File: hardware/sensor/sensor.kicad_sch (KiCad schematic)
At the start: 12 parts

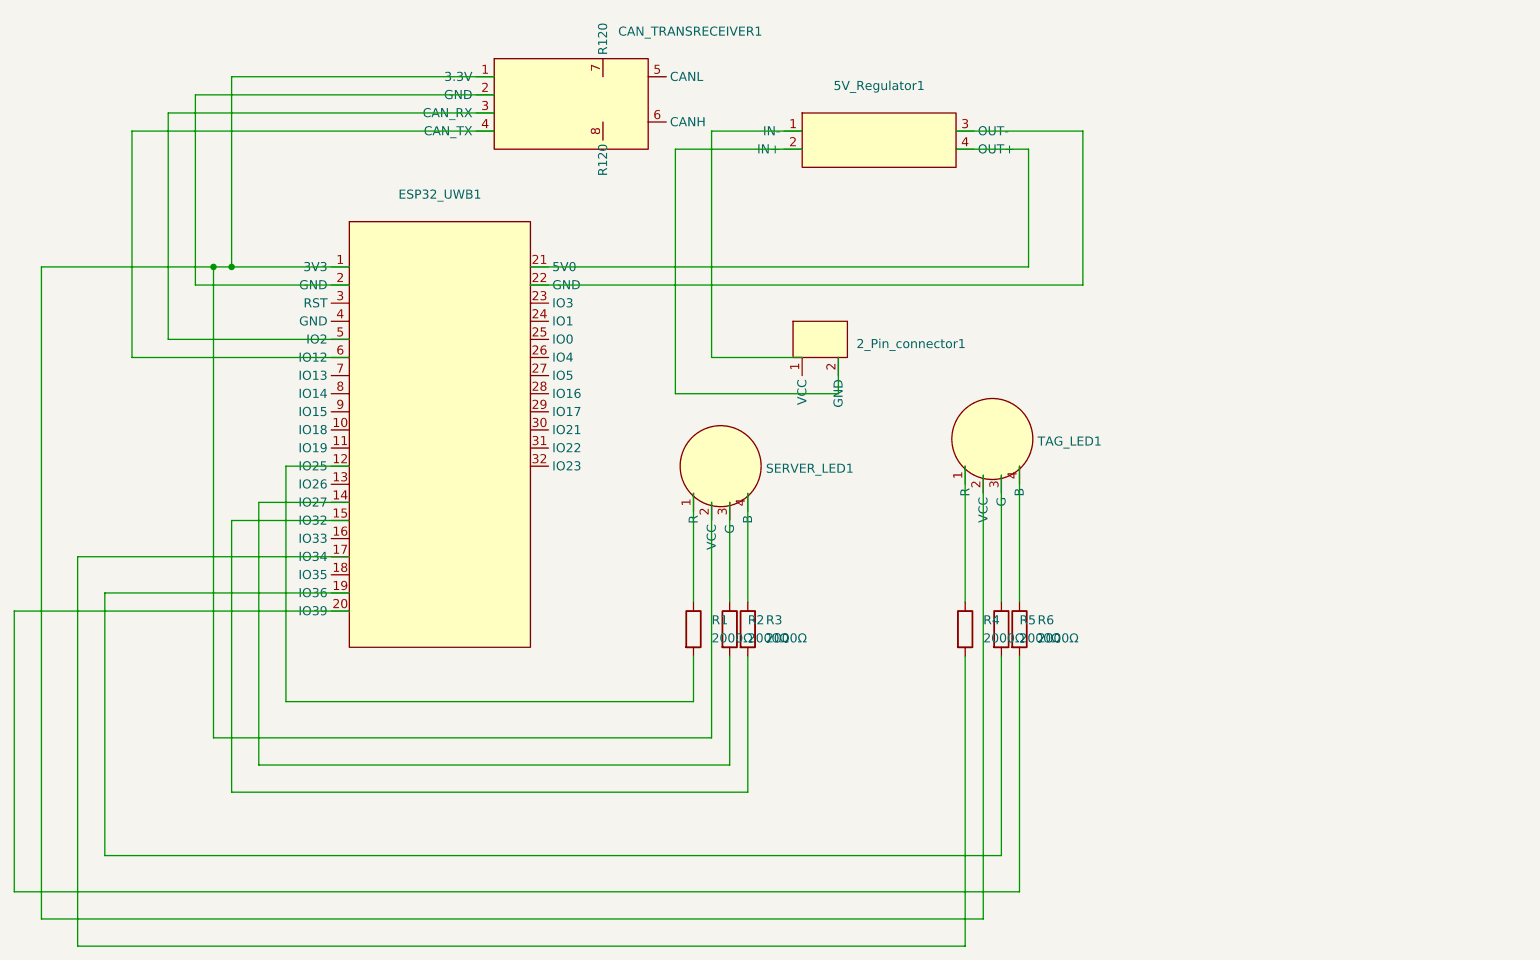
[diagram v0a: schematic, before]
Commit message: KiCad footprint library: Refactor footprint names.
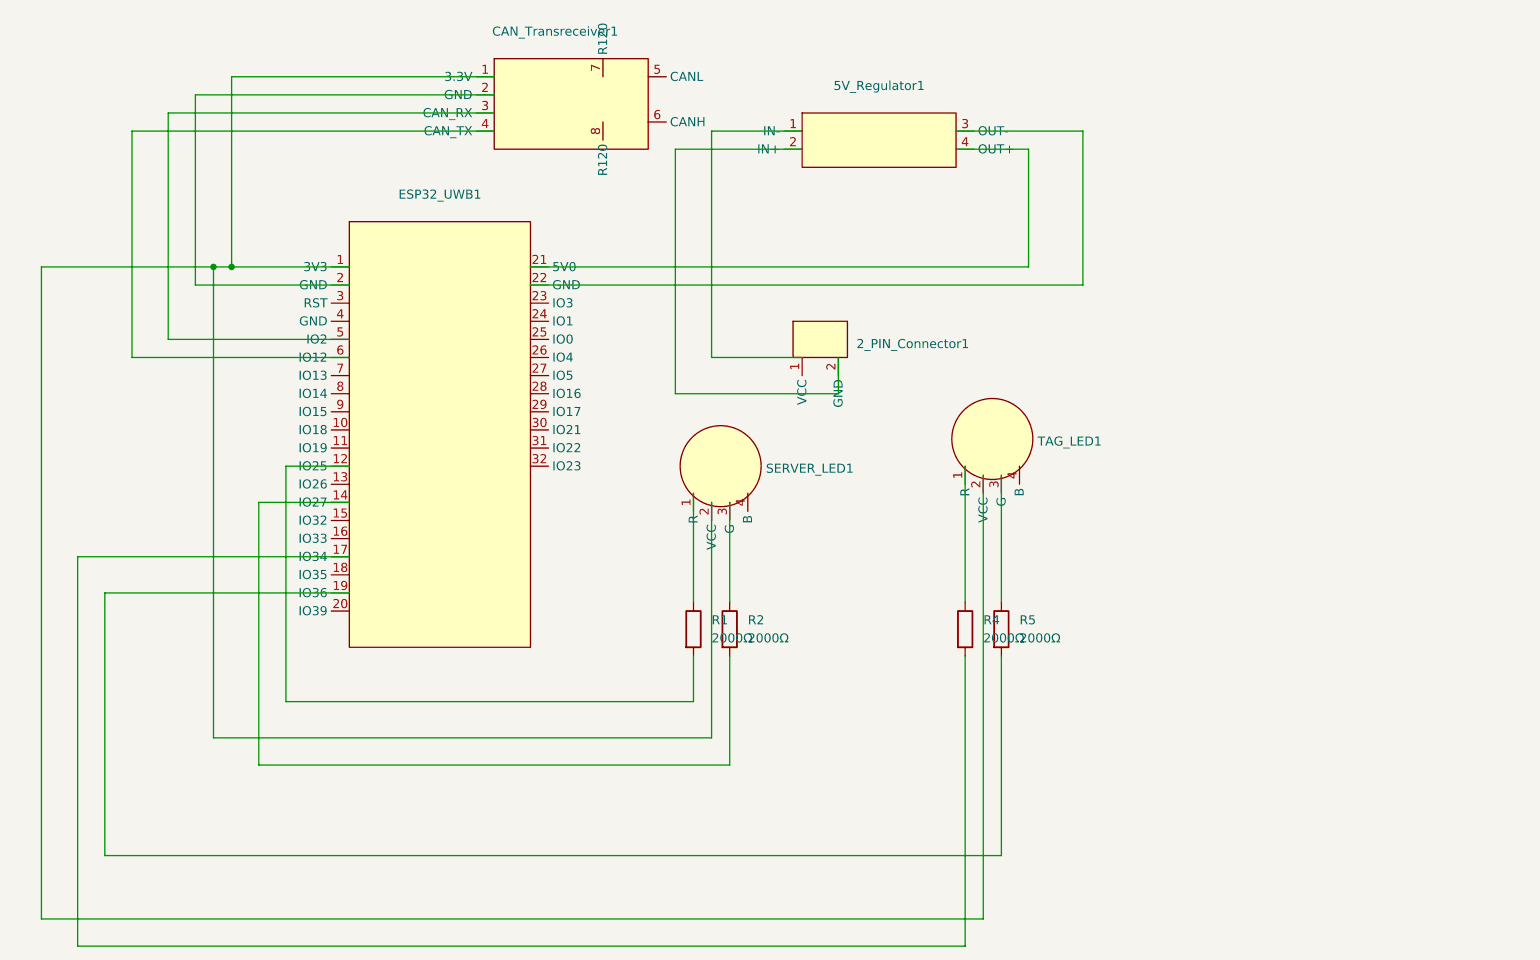
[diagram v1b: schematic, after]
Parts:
- removed R3, R6: 2000Ω, autocam:resistor, symbol Device:R
- 2_PIN_Connector1: renamed from 2_Pin_connector1; footprint autocam:2-pin connector -> Autocam:2-PIN Connector
- 5V_Regulator1: footprint autocam:MP1584EN 5V regulator -> Autocam:MP1584EN 5V Regulator
- CAN_Transreceiver1: renamed from CAN_TRANSRECEIVER1; footprint autocam:Waveshare CAN transreceiver -> Autocam:Waveshare CAN Transreceiver
- ESP32_UWB1: footprint autocam:esp32_uwb1000 -> Autocam:Makersfab ESP32 UWB
- R1, R2, R4, R5: footprint autocam:resistor -> Autocam:Simple Resistor
- SERVER_LED1, TAG_LED1: footprint autocam:Anode REB LED (round) -> Autocam:Anode RGB LED (Round)
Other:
- title: (none) -> Autocam Sensor

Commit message: hardware/server: Add server PCB.
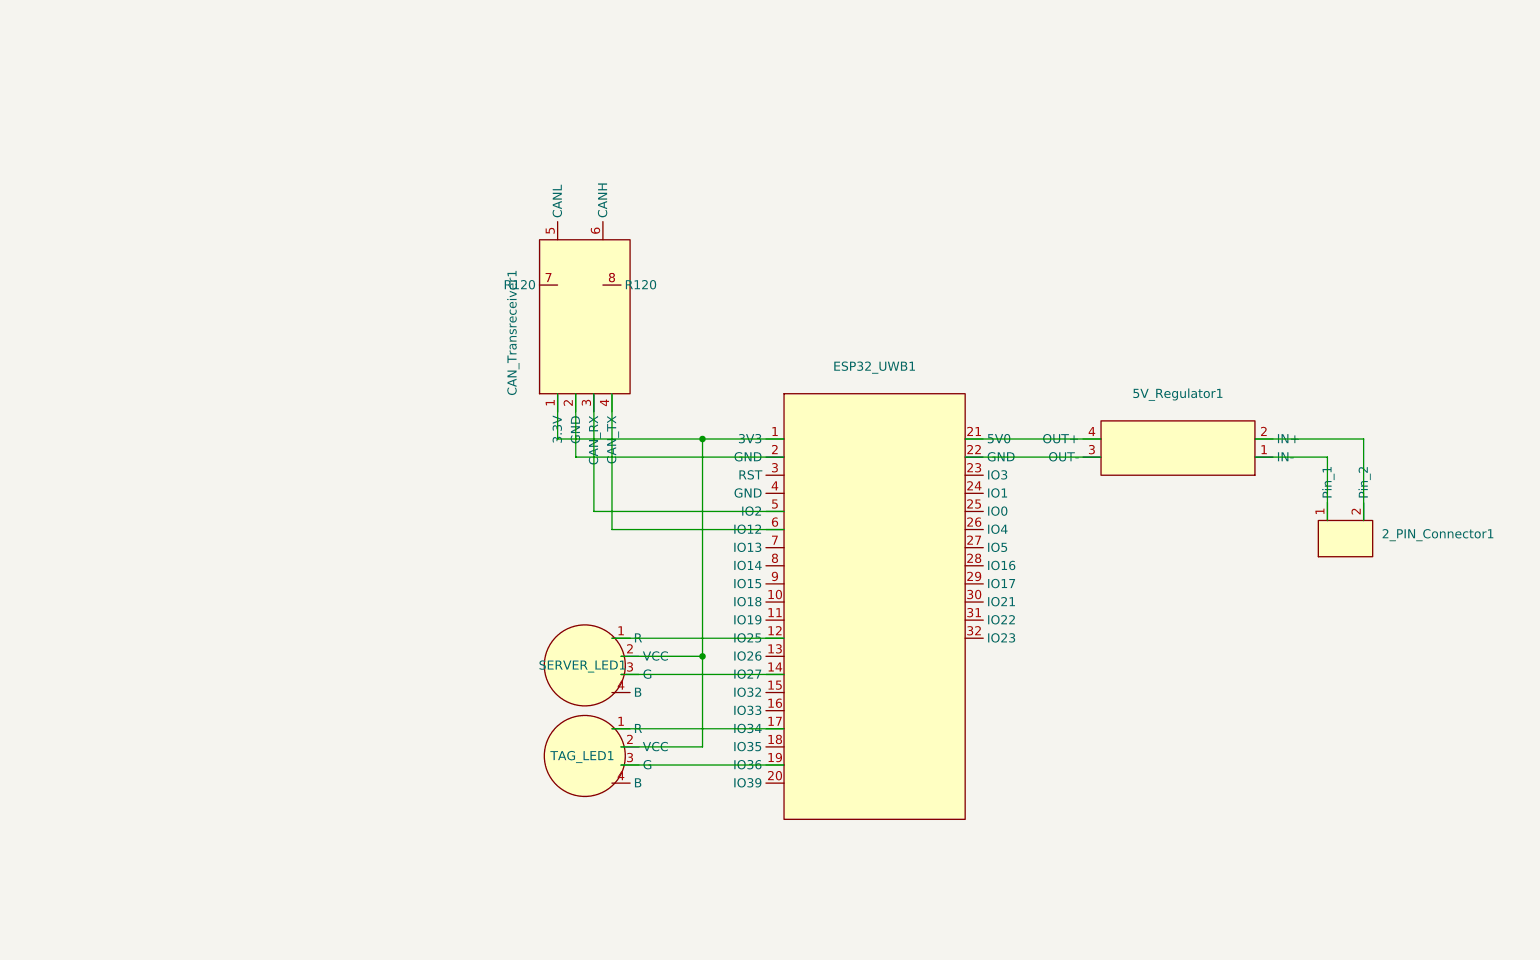
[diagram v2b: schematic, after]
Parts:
- removed 2_PIN_Connector1: ~, Autocam:2-PIN Connector, symbol autocam:2_pin_connector
- removed R1, R2, R4, R5: 2000Ω, Autocam:Simple Resistor, symbol Device:R
- added 2_PIN_Connector1: ~, Autocam:2-PIN Connector, symbol Autocam:2_PIN_Connector
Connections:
- net at 5V_Regulator1.1 (IN-): now also 2_PIN_Connector1.1 (Pin_1)
- net at 5V_Regulator1.2 (IN+): now also 2_PIN_Connector1.2 (Pin_2)
- net at SERVER_LED1.1 (R): now also ESP32_UWB1.12 (IO25)
- net at TAG_LED1.1 (R): now also ESP32_UWB1.17 (IO34)
- net at TAG_LED1.3 (G): now also ESP32_UWB1.19 (IO36)
- net at SERVER_LED1.3 (G): now also ESP32_UWB1.14 (IO27)
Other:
- moved on the sheet: 5V_Regulator1, CAN_Transreceiver1, ESP32_UWB1, SERVER_LED1, TAG_LED1

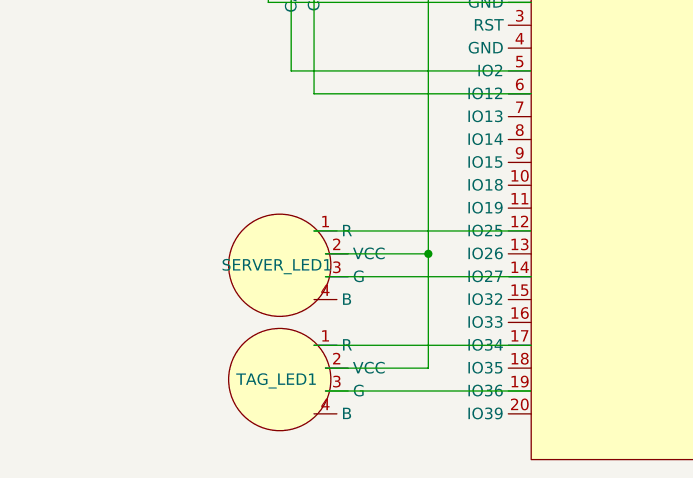
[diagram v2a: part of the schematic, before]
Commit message: hardware: Add more footprint measurement.
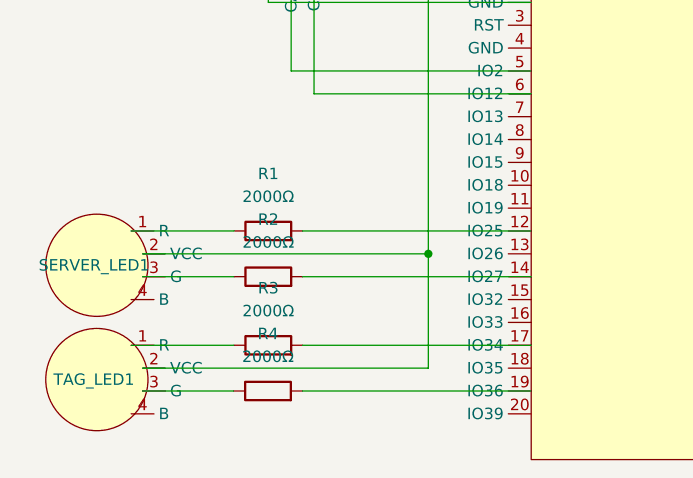
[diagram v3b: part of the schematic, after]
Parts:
- added R1, R2, R3, R4: 2000Ω, Autocam:Simple Resistor, symbol Autocam:Simple Resistor
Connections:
- net at TAG_LED1.1 (R): now also R3.1; no longer ESP32_UWB1.17 (IO34)
- net at TAG_LED1.3 (G): now also R4.1; no longer ESP32_UWB1.19 (IO36)
- net at SERVER_LED1.1 (R): now also R1.1; no longer ESP32_UWB1.12 (IO25)
- net at SERVER_LED1.3 (G): now also R2.1; no longer ESP32_UWB1.14 (IO27)
- new net: ESP32_UWB1.17 (IO34), R3.2
- new net: ESP32_UWB1.19 (IO36), R4.2
- new net: ESP32_UWB1.12 (IO25), R1.2
- new net: ESP32_UWB1.14 (IO27), R2.2
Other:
- moved on the sheet: SERVER_LED1, TAG_LED1

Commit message: hardware: Add remote PCB.
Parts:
- SERVER_LED1: value ~ -> SERVER
- TAG_LED1: value ~ -> TAG
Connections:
- net at R3.2: now also ESP32_UWB1.15 (IO32); no longer ESP32_UWB1.17 (IO34)
- net at R4.2: now also ESP32_UWB1.16 (IO33); no longer ESP32_UWB1.19 (IO36)
- net at ESP32_UWB1.13 (IO26): now also R2.2
- net at ESP32_UWB1.14 (IO27): no longer R2.2
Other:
- moved on the sheet: R1, R2, R3, R4
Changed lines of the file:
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@@
 	)
 	(junction
-		(at 125.73 120.65)
+		(at 105.41 90.17)
 		(diameter 0)
 		(color 0 0 0 0)
 	)
 	(junction
-		(at 125.73 90.17)
+		(at 101.6 120.65)
 		(diameter 0)
 		(color 0 0 0 0)
@@
 	(wire
 		(pts
-			(xy 93.98 120.65) (xy 125.73 120.65)
-		)
-		(stroke
-			(width 0)
-			(type default)
-		)
-	)
-	(wire
-		(pts
-			(xy 125.73 90.17) (xy 125.73 120.65)
+			(xy 93.98 120.65) (xy 101.6 120.65)
+		)
+		(stroke
+			(width 0)
+			(type default)
+		)
+	)
+	(wire
+		(pts
+			(xy 101.6 90.17) (xy 101.6 120.65)
 		)
 		(stroke
@@
 	(wire
 		(pts
-			(xy 125.73 90.17) (xy 137.16 90.17)
+			(xy 104.14 125.73) (xy 104.14 130.81)
 		)
 		(stroke
@@
 	(wire
 		(pts
-			(xy 92.71 130.81) (xy 104.14 130.81)
-		)
-		(stroke
-			(width 0)
-			(type default)
-		)
-	)
-	(wire
-		(pts
 			(xy 110.49 100.33) (xy 137.16 100.33)
 		)
@@
 	(wire
 		(pts
-			(xy 93.98 133.35) (xy 125.73 133.35)
-		)
-		(stroke
-			(width 0)
-			(type default)
-		)
-	)
-	(wire
-		(pts
-			(xy 111.76 123.19) (xy 137.16 123.19)
+			(xy 93.98 133.35) (xy 101.6 133.35)
 		)
 		(stroke
@@
 	(wire
 		(pts
-			(xy 111.7236 135.89) (xy 137.16 135.89)
+			(xy 106.68 128.27) (xy 106.68 135.89)
+		)
+		(stroke
+			(width 0)
+			(type default)
+		)
+	)
+	(wire
+		(pts
+			(xy 104.14 130.81) (xy 92.71 130.81)
+		)
+		(stroke
+			(width 0)
+			(type default)
+		)
+	)
+	(wire
+		(pts
+			(xy 105.41 90.17) (xy 137.16 90.17)
+		)
+		(stroke
+			(width 0)
+			(type default)
+		)
+	)
+	(wire
+		(pts
+			(xy 101.6 90.17) (xy 105.41 90.17)
 		)
 		(stroke
@@
 	(wire
 		(pts
-			(xy 111.76 118.11) (xy 137.16 118.11)
+			(xy 125.73 128.27) (xy 137.16 128.27)
+		)
+		(stroke
+			(width 0)
+			(type default)
+		)
+	)
+	(wire
+		(pts
+			(xy 125.73 120.65) (xy 137.16 120.65)
+		)
+		(stroke
+			(width 0)
+			(type default)
+		)
+	)
+	(wire
+		(pts
+			(xy 125.73 125.73) (xy 137.16 125.73)
+		)
+		(stroke
+			(width 0)
+			(type default)
+		)
+	)
+	(wire
+		(pts
+			(xy 125.73 118.11) (xy 137.16 118.11)
 		)
 		(stroke
@@
 	(wire
 		(pts
+			(xy 118.11 128.27) (xy 106.68 128.27)
+		)
+		(stroke
+			(width 0)
+			(type default)
+		)
+	)
+	(wire
+		(pts
+			(xy 102.87 120.65) (xy 102.87 123.19)
+		)
+		(stroke
+			(width 0)
+			(type default)
+		)
+	)
+	(wire
+		(pts
 			(xy 113.03 83.82) (xy 113.03 102.87)
 		)
@@
 	(wire
 		(pts
-			(xy 93.98 135.89) (xy 104.1036 135.89)
-		)
-		(stroke
-			(width 0)
-			(type default)
-		)
-	)
-	(wire
-		(pts
 			(xy 213.36 101.6) (xy 213.36 92.71)
 		)
@@
 	(wire
 		(pts
-			(xy 111.76 130.81) (xy 137.16 130.81)
-		)
-		(stroke
-			(width 0)
-			(type default)
-		)
-	)
-	(wire
-		(pts
-			(xy 105.41 90.17) (xy 125.73 90.17)
+			(xy 118.11 125.73) (xy 104.14 125.73)
 		)
 		(stroke
@@
 	(wire
 		(pts
-			(xy 92.71 118.11) (xy 104.14 118.11)
-		)
-		(stroke
-			(width 0)
-			(type default)
-		)
-	)
-	(wire
-		(pts
-			(xy 125.73 120.65) (xy 125.73 133.35)
-		)
-		(stroke
-			(width 0)
-			(type default)
-		)
-	)
-	(wire
-		(pts
-			(xy 93.98 123.19) (xy 104.14 123.19)
+			(xy 92.71 118.11) (xy 118.11 118.11)
+		)
+		(stroke
+			(width 0)
+			(type default)
+		)
+	)
+	(wire
+		(pts
+			(xy 101.6 120.65) (xy 101.6 133.35)
+		)
+		(stroke
+			(width 0)
+			(type default)
+		)
+	)
+	(wire
+		(pts
+			(xy 106.68 135.89) (xy 93.98 135.89)
+		)
+		(stroke
+			(width 0)
+			(type default)
+		)
+	)
+	(wire
+		(pts
+			(xy 102.87 120.65) (xy 118.11 120.65)
 		)
 		(stroke
@@
 		(pts
 			(xy 162.56 90.17) (xy 181.61 90.17)
+		)
+		(stroke
+			(width 0)
+			(type default)
+		)
+	)
+	(wire
+		(pts
+			(xy 102.87 123.19) (xy 93.98 123.19)
 		)
 		(stroke
@@
 	(symbol
 		(lib_id "Autocam:Simple Resistor")
-		(at 107.95 130.81 90)
+		(at 121.92 125.73 90)
 		(unit 1)
 		(exclude_from_sim no)
@@
 		(dnp no)
 		(property "Reference" "R3"
-			(at 107.95 124.46 90)
+			(at 126.492 124.714 90)
 			(effects
 				(font
@@
 		)
 		(property "Value" "2000Ω"
-			(at 107.95 127 90)
+			(at 121.92 125.73 90)
 			(effects
 				(font
@@
 		)
 		(property "Footprint" "Autocam:Simple Resistor"
-			(at 107.95 132.588 90)
+			(at 121.92 127.508 90)
 			(effects
 				(font
@@
 		)
 		(property "Datasheet" "~"
-			(at 107.95 130.81 0)
+			(at 121.92 125.73 0)
 			(effects
 				(font
@@
 		)
 		(property "Description" "Resistor"
-			(at 107.95 130.81 0)
+			(at 121.92 125.73 0)
 			(effects
 				(font
@@
 			)
 		)
-		(property "Value" "~"
-			(at 97.79 133.35 90)
+		(property "Value" "TAG"
+			(at 86.868 142.24 90)
 			(effects
 				(font
@@
 			)
 		)
-		(property "Value" "~"
-			(at 91.1402 128.27 0)
+		(property "Value" "SERVER"
+			(at 92.456 113.792 90)
 			(effects
 				(font
@@
 	(symbol
 		(lib_id "Autocam:Simple Resistor")
-		(at 107.9136 135.89 90)
+		(at 121.92 128.27 90)
 		(unit 1)
 		(exclude_from_sim no)
@@
 		(dnp no)
 		(property "Reference" "R4"
-			(at 107.9136 129.54 90)
+			(at 126.5284 127.254 90)
 			(effects
 				(font
@@
 		)
 		(property "Value" "2000Ω"
-			(at 107.9136 132.08 90)
+			(at 121.9564 128.27 90)
 			(effects
 				(font
@@
 		)
 		(property "Footprint" "Autocam:Simple Resistor"
-			(at 107.9136 137.668 90)
+			(at 121.92 130.048 90)
 			(effects
 				(font
@@
 		)
 		(property "Datasheet" "~"
-			(at 107.9136 135.89 0)
+			(at 121.92 128.27 0)
 			(effects
 				(font
@@
 		)
 		(property "Description" "Resistor"
-			(at 107.9136 135.89 0)
+			(at 121.92 128.27 0)
 			(effects
 				(font
@@
 	(symbol
 		(lib_id "Autocam:Simple Resistor")
-		(at 107.95 118.11 90)
+		(at 121.92 118.11 90)
 		(unit 1)
 		(exclude_from_sim no)
@@
 		(dnp no)
 		(property "Reference" "R1"
-			(at 107.95 111.76 90)
+			(at 126.492 117.094 90)
 			(effects
 				(font
@@
 		)
 		(property "Value" "2000Ω"
-			(at 107.95 114.3 90)
+			(at 121.92 117.856 90)
 			(effects
 				(font
@@
 		)
 		(property "Footprint" "Autocam:Simple Resistor"
-			(at 107.95 119.888 90)
+			(at 121.92 119.888 90)
 			(effects
 				(font
@@
 		)
 		(property "Datasheet" "~"
-			(at 107.95 118.11 0)
+			(at 121.92 118.11 0)
 			(effects
 				(font
@@
 		)
 		(property "Description" "Resistor"
-			(at 107.95 118.11 0)
+			(at 121.92 118.11 0)
 			(effects
 				(font
@@
 	(symbol
 		(lib_id "Autocam:Simple Resistor")
-		(at 107.95 123.19 90)
+		(at 121.92 120.65 90)
 		(unit 1)
 		(exclude_from_sim no)
@@
 		(dnp no)
 		(property "Reference" "R2"
-			(at 107.95 116.84 90)
+			(at 126.492 119.634 90)
 			(effects
 				(font
@@
 		)
 		(property "Value" "2000Ω"
-			(at 107.95 119.38 90)
+			(at 121.92 120.65 90)
 			(effects
 				(font
@@
 		)
 		(property "Footprint" "Autocam:Simple Resistor"
-			(at 107.95 124.968 90)
+			(at 121.92 122.428 90)
 			(effects
 				(font
@@
 		)
 		(property "Datasheet" "~"
-			(at 107.95 123.19 0)
+			(at 121.92 120.65 0)
 			(effects
 				(font
@@
 		)
 		(property "Description" "Resistor"
-			(at 107.95 123.19 0)
-			(effects
-				(font
+			(at 121.92 120.65 0)
+			(effects
+				(font

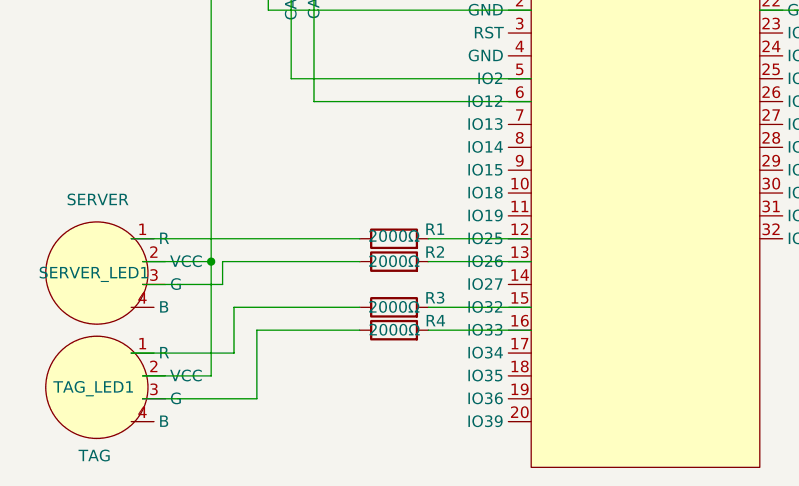
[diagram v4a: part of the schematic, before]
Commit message: hardware: Increase the LED resistor from 2000Ω to 10KΩ.
To reduce the power consumption.
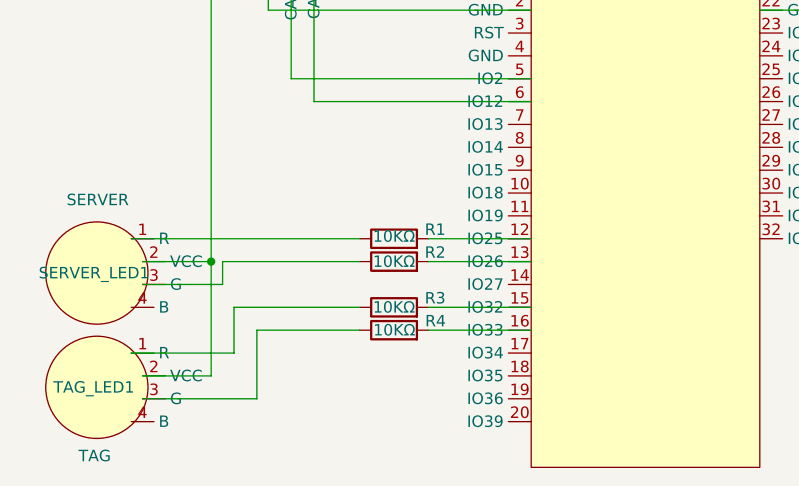
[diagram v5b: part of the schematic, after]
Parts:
- R1, R2, R3, R4: value 2000Ω -> 10KΩ
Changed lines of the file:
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@@
 			)
 		)
-		(property "Value" "2000Ω"
+		(property "Value" "10KΩ"
 			(at 121.92 125.73 90)
 			(effects
@@
 			)
 		)
-		(property "Value" "2000Ω"
+		(property "Value" "10KΩ"
 			(at 121.9564 128.27 90)
 			(effects
@@
 			)
 		)
-		(property "Value" "2000Ω"
+		(property "Value" "10KΩ"
 			(at 121.92 117.856 90)
 			(effects
@@
 			)
 		)
-		(property "Value" "2000Ω"
+		(property "Value" "10KΩ"
 			(at 121.92 120.65 90)
 			(effects
